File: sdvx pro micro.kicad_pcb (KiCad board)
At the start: 2 copper layers, 124 x 44 mm, 14 parts

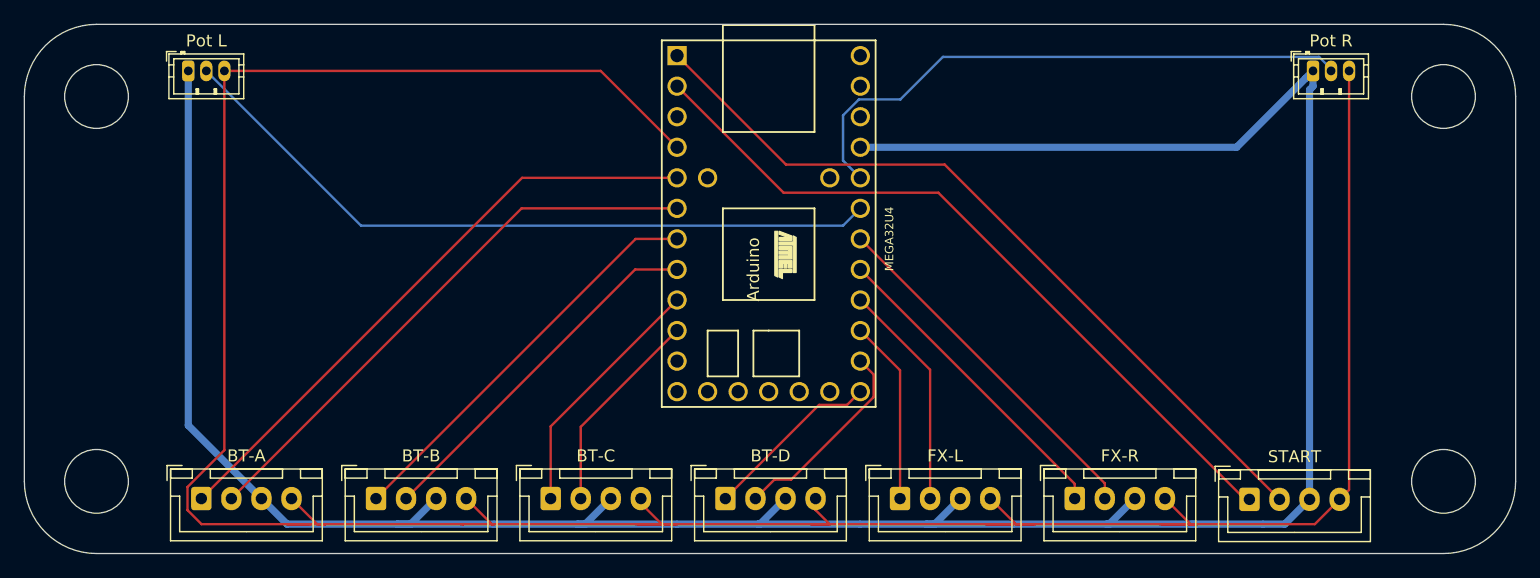
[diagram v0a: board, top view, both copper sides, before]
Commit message: added capacitor to 5V line to reduce capacitor noise. swapped JST-ZH for JST-PH
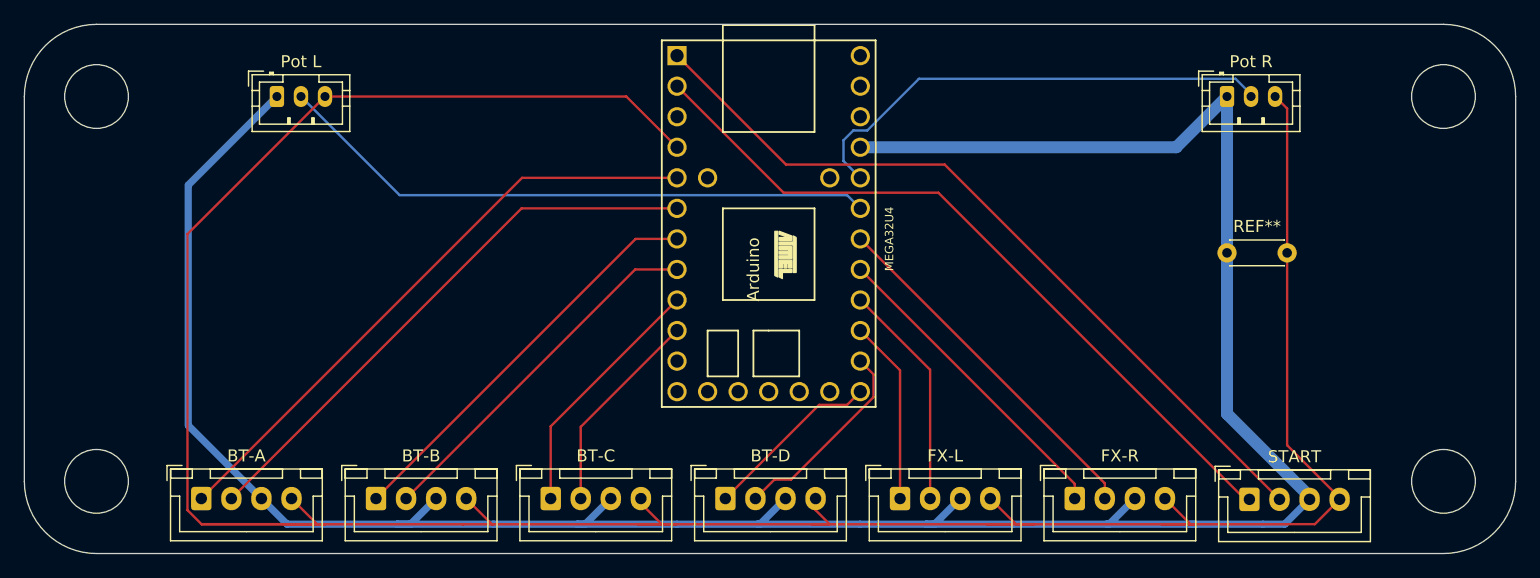
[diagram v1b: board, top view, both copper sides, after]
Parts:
- added REF**: C_Disc_D4.3mm_W1.9mm_P5.00mm, Capacitor_THT:C_Disc_D4.3mm_W1.9mm_P5.00mm, F.Cu at (94.0, 13.0)
- Pot L: value JST_ZH_B3B-ZR_1x03_P1.50mm_Vertical -> JST_PH_B3B-PH-K_1x03_P2.00mm_Vertical; footprint Connector_JST:JST_ZH_B3B-ZR_1x03_P1.50mm_Vertical -> Connector_JST:JST_PH_B3B-PH-K_1x03_P2.00mm_Vertical
- Pot R: value JST_ZH_B3B-ZR_1x03_P1.50mm_Vertical -> JST_PH_B3B-PH-K_1x03_P2.00mm_Vertical; footprint Connector_JST:JST_ZH_B3B-ZR_1x03_P1.50mm_Vertical -> Connector_JST:JST_PH_B3B-PH-K_1x03_P2.00mm_Vertical
- moved Pot L 7.67 mm to (15.0, 0.00)
- moved Pot R 7.46 mm to (94.0, 0.00)
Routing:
- net EncData: track 109.8 -> 90.8 mm
- net 5V: track 221.5 -> 215.1 mm
- net Ground: track 243.8 -> 245.9 mm
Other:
- board text added: "JST-PH 3 Pin"
- board text removed: "JST-ZH 3 Pin"

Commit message: Increased GND track width, moved capacitor closer to VCC
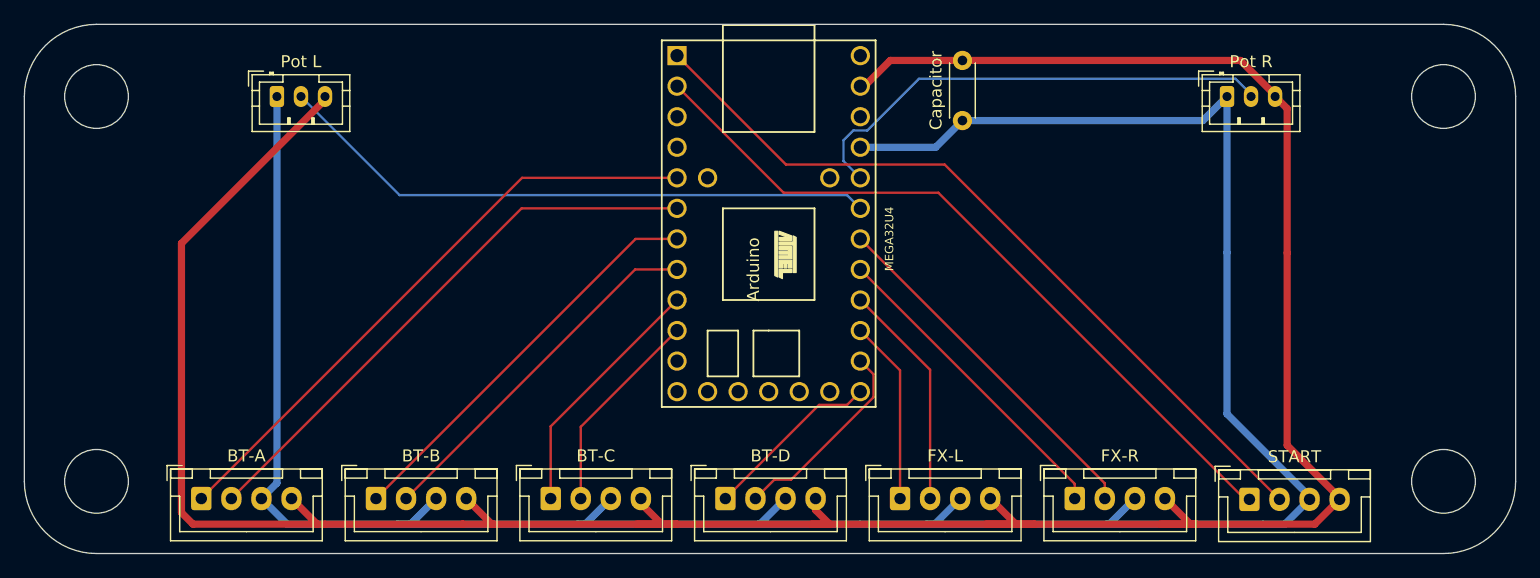
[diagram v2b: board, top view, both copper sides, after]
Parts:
- removed the REF** at (94.0, 13.0)
- added Capacitor: C_Disc_D4.3mm_W1.9mm_P5.00mm, Capacitor_THT:C_Disc_D4.3mm_W1.9mm_P5.00mm, F.Cu at (72.0, 2.00)
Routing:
- net Ground: track 245.9 -> 239.6 mm
- net 5V: track 215.1 -> 210.0 mm
